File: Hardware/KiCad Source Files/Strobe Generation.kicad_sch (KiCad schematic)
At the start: 23 parts, among them Q1 IRLU024NPBF, Q2 IRLU024NPBF, Q3 Q_NMOS

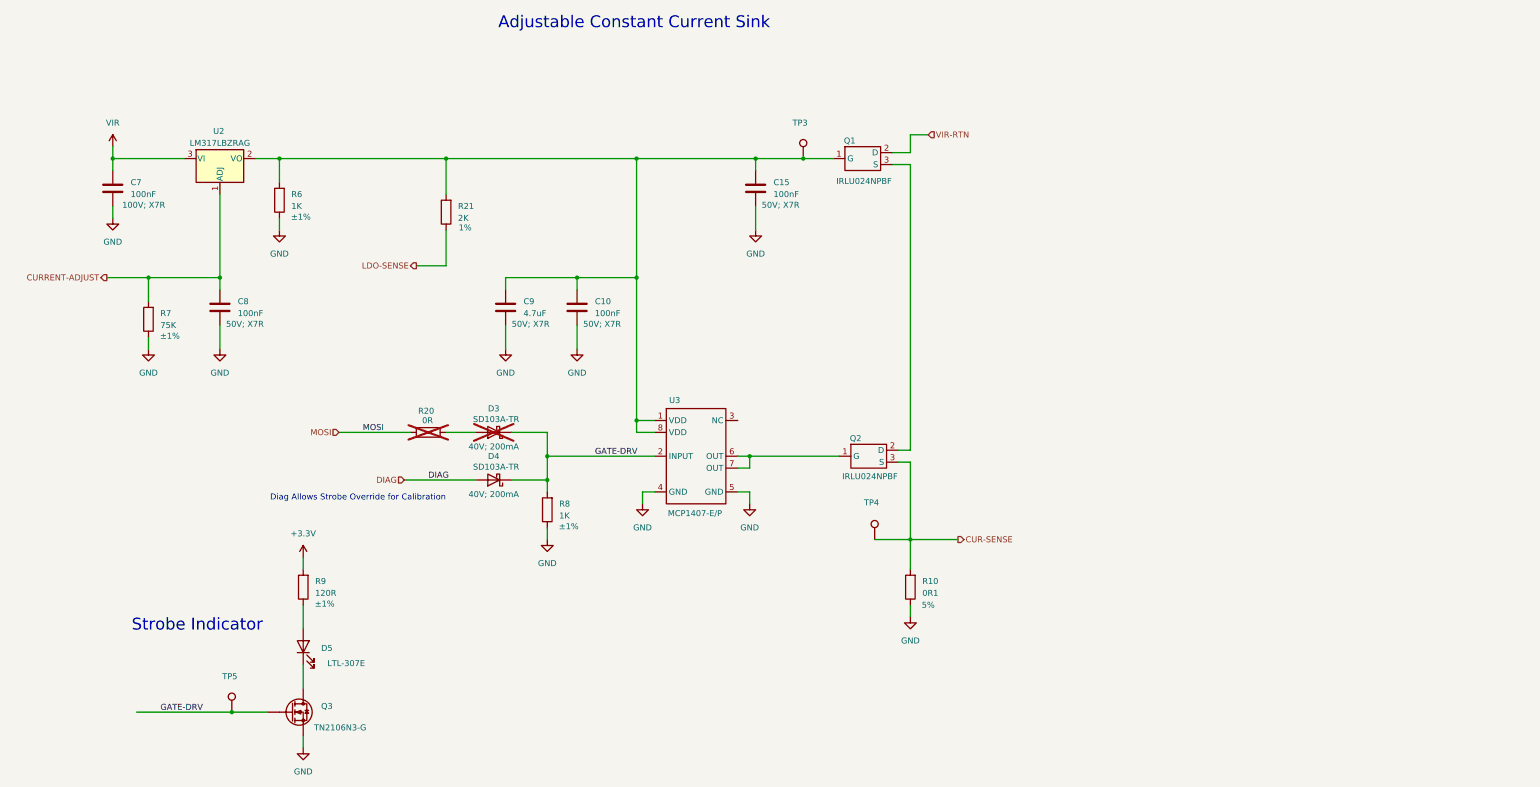
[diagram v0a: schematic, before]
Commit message: V3 connector board: strobe pulse limiter, USB-C fixes, boost protection
Mechanical: board outline, all mounting/tab/breakaway holes and every
existing part position are unchanged (checked against the previous revision);
all new parts are on the top side and no taller than existing parts.
PiTrac software compatibility: the LED current-control circuit and the
DAC/ADC/DIAG interface used by strobe_calibration_manager.py are unchanged.

Strobe (CC Sink sheet)
- AC-coupled pulse limiter: TRIG (DIAG/MOSI via D3/D4) -> C16 220nF ->
  GATE-DRV, R28 10K to GND (tau 2.2 ms). 8.7-130 us strobes and the
  calibration pulse pass (guaranteed >= ~0.38 ms by the MCP1407 input
  limits); a stuck-high DIAG turns the driver off after ~1.7 ms typical,
  <= ~2.8 ms worst case, so 10 A can no longer be held on.

USB-C (Connectors sheet, USB4085-GF-A footprint)
- J2/J5 feed 5 V to the Pis: add 10K Rp on CC1/CC2 (R24-R27, 1206).
- Footprint rebuilt to GCT's land pattern (16 plated 0.40/0.66 mm pins).
  The old VBUS/GND pads had 0.1 mm top-side copper (annular-ring DRC
  errors; Pi supply current only reached them via the barrel/bottom pad).

Boost (Power sheet)
- F1 MF-MSMF050-2 polyfuse in the boost input only (+5V_BST: C1/C2/C3/R1/
  U1); PCB: +5V_BST F.Cu island, +5V B.Cu bridge keeps the Pi feed width.
- D16 P4SMA39CA clamp on VIR (open-feedback fault; relies on F1).
- R5 2K49 -> 10K (was ~0.45 W in a 1/4 W resistor).

Housekeeping
- Project sym/fp-lib-tables; USB4085-GF-A added to the symbol library;
  pin types for custom parts; locally modified Q_NPN/Q_NMOS/LED moved into
  the project library (Q_NPN_EBC, Q_NMOS_SGD, LED_ThermalPad) to keep their
  numeric pinouts; no-connect flags; PWR_FLAGs; GATE-DRV wire to Q3 fixed.
- ERC pin map (project-wide): open emitter on a power rail allowed
  (MC33063 SwE to GND).
- Add V3 Connector Only.kicad_pro (board had no rules; DRC used defaults).
- Breakaway holes marked board-only.
- Regenerated Gerber/drill zips, BOM and centroid CSVs (same for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
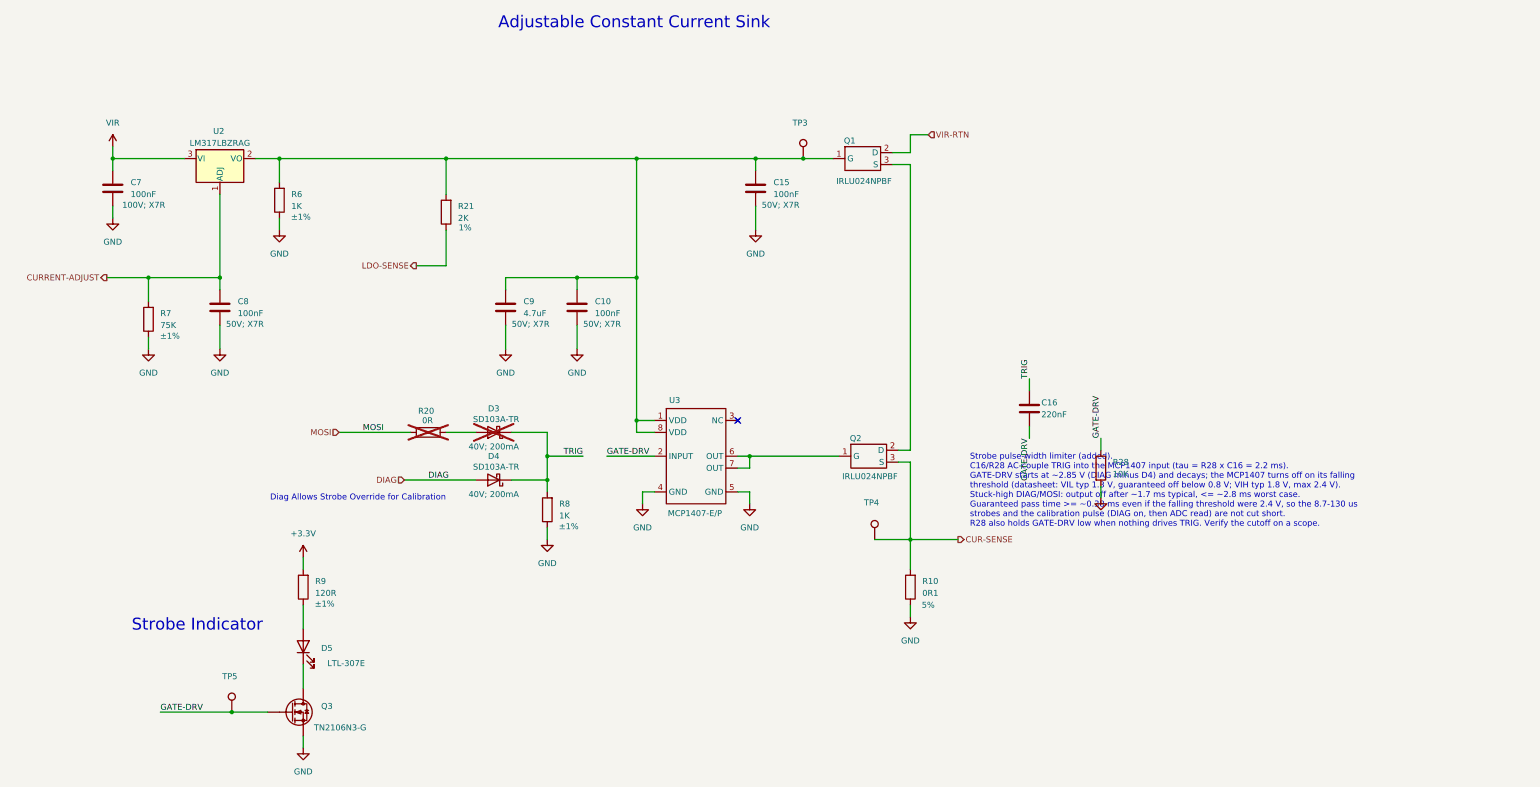
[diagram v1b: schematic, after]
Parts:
- added C16: 220nF, Capacitor_THT:C_Disc_D4.3mm_W1.9mm_P5.00mm, symbol Device:C
- added R28: 10K, Resistor_THT:R_Axial_DIN0207_L6.3mm_D2.5mm_P2.54mm_Vertical, symbol Device:R
- Q3: symbol Device:Q_NMOS -> Pi Connector Parts:Q_NMOS_SGD
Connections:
- net GATE-DRV: now also C16.2, R28.1; no longer D3.1 (K), D4.1 (K), R8.2
- net GND: now also R28.2
- new net TRIG: C16.1, D3.1 (K), D4.1 (K), R8.2
- no-connect marks 0 -> 1
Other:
- note added: "Strobe pulse-width limiter (added). C16/R28 AC-couple TRIG into the MCP1407 input (tau = R28 x C16 = 2.2 ms). GATE-DRV starts at ~2.85 V (DIAG minus D4) and decays; the MCP1407 turns off on its falling threshold (datasheet: VIL typ 1.3 V, guaranteed off below 0.8 V; VIH typ 1.8 V, max 2.4 V). Stuck-high DIAG/MOSI: output off after ~1.7 ms typical, <= ~2.8 ms worst case. Guaranteed pass time >= ~0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"

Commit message: C16: use an orderable part (K224K20X7RF5UH5, 220nF 50V X7R)
K224K15X7RF5UH5 isn't listed by any distributor; the "20" (50 V) code is the
real 220 nF part in this Vishay K series (DigiKey 2356767, element14
2860121). Footprint moved to C_Disc_D5.1mm_W3.2mm_P5.00mm, the one already
used for C2 (1 uF in the same series), so the body fits.
Outputs regenerated; ERC/DRC unchanged (0 errors), geometry unchanged.

Co-Authored-By: Claude Opus 5.5 <noreply@anthropic.com>
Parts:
- C16: footprint Capacitor_THT:C_Disc_D4.3mm_W1.9mm_P5.00mm -> Capacitor_THT:C_Disc_D5.1mm_W3.2mm_P5.00mm; Part Number K224K15X7RF5UH5 -> K224K20X7RF5UH5
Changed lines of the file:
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@@
 			)
 		)
-		(property "Footprint" "Capacitor_THT:C_Disc_D4.3mm_W1.9mm_P5.00mm"
+		(property "Footprint" "Capacitor_THT:C_Disc_D5.1mm_W3.2mm_P5.00mm"
 			(at 241.3 104.14 0)
 			(effects
@@
 			)
 		)
-		(property "Part Number" "K224K15X7RF5UH5"
+		(property "Part Number" "K224K20X7RF5UH5"
 			(at 241.3 104.14 0)
 			(effects

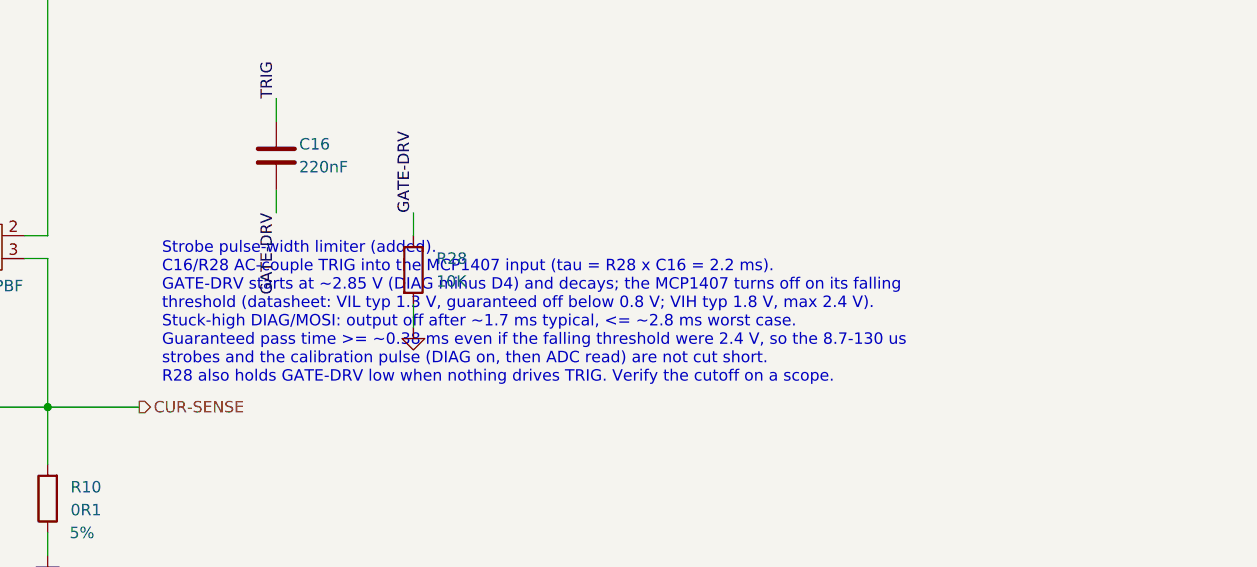
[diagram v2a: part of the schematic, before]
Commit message: Address PR review: R5 part number, timing bounds, library defaults, ERC scope
- R5: PCB Part Number field still named the old MFR-25FTE52-2K49 on both
  boards; now MFR-25FRF52-10K, matching the schematic and BOM. (The stage-A
  update changed the value but not the BOM fields; no other part drifted.)
- Limiter note: worst-case bounds now include R28 1%, C16 +-10% plus X7R
  drift and a 2.7-2.95 V start level: cutoff <= ~3.2 ms, pass >= ~0.2 ms
  worst case (~1.7 ms typical for both).
- USB-C labels: "3A advertised (CC), 5A max" instead of "5A" — the Rp
  pull-ups advertise Type-C 3 A; the connector/copper are rated 5 A.
- Project library: default references Q4/Q1/D1 -> Q/Q/D; LED_ThermalPad
  default footprint -> Pi Connector Parts:VSMA1085400 (was an unresolvable
  Library:SST-10-IRD-B90H-S810). Sheet caches updated identically.
- ERC: revert the project-wide open-emitter/power-output relaxation and add a
  single exclusion for U1 pin 2 (MC33063 SwE to GND).
- V3 Connector Only.kicad_pro: own export folder and BOM file name.
- Regenerated Gerber zips and schematic PDF (BOM/centroid unchanged).

ERC 0 (1 intended exclusion). DRC both boards: 0 errors.

Co-Authored-By: Claude Opus 5.5 <noreply@anthropic.com>
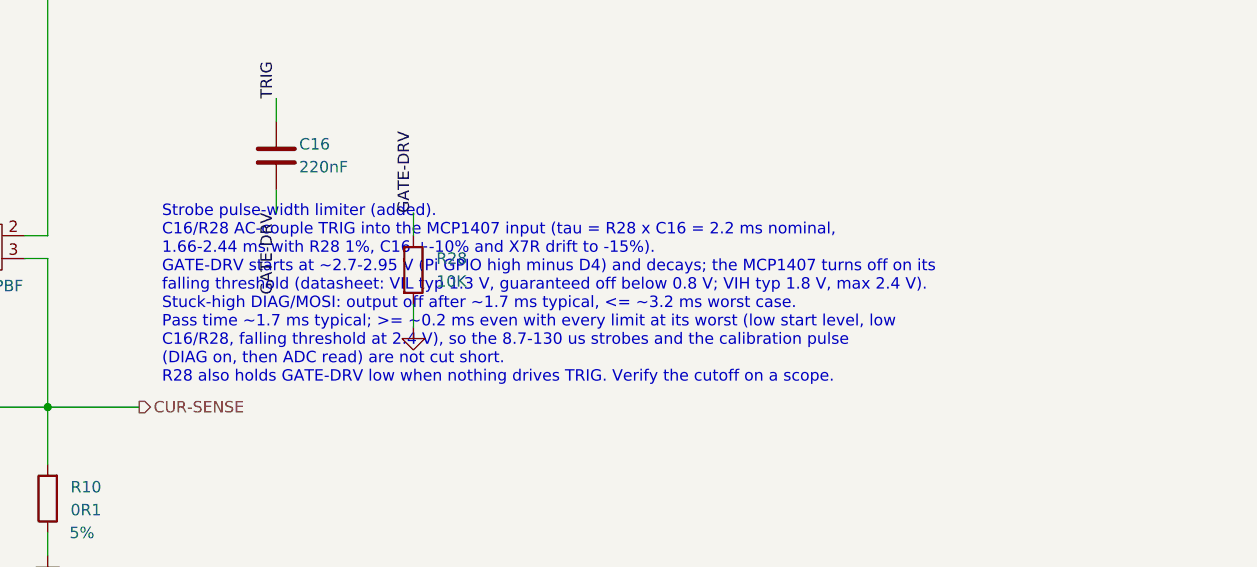
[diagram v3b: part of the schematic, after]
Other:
- note added: "Strobe pulse-width limiter (added). C16/R28 AC-couple TRIG into the MCP1407 input (tau = R28 x C16 = 2.2 ms nominal, 1.66-2.44 ms with R28 1%, C16 +-10% and X7R drift to -15%). GATE-DRV starts at ~2.7-2.95 V (Pi GPIO high minus D4) and decays; the MCP1407 turns off on its falling threshold (datasheet: VIL typ 1.3 V, guaranteed off below 0.8 V; VIH typ 1.8 V, max 2.4 V). Stuck-high DIAG/MOSI: outp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"
- note removed: "Strobe pulse-width limiter (added). C16/R28 AC-couple TRIG into the MCP1407 input (tau = R28 x C16 = 2.2 ms). GATE-DRV starts at ~2.85 V (DIAG minus D4) and decays; the MCP1407 turns off on its falling threshold (datasheet: VIL typ 1.3 V, guaranteed off below 0.8 V; VIH typ 1.8 V, max 2.4 V). Stuck-high DIAG/MOSI: output off after ~1.7 ms typical, <= ~2.8 ms worst case. Guaranteed pass time >= ~0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"
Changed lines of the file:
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@@
 		)
 	)
-	(text "Strobe pulse-width limiter (added).
-C16/R28 AC-couple TRIG into the MCP1407 input (tau = R28 x C16 = 2.2 ms).
-GATE-DRV starts at ~2.85 V (DIAG minus D4) and decays; the MCP1407 turns off on its falling
-threshold (datasheet: VIL typ 1.3 V, guaranteed off below 0.8 V; VIH typ 1.8 V, max 2.4 V).
-Stuck-high DIAG/MOSI: output off after ~1.7 ms typical, <= ~2.8 ms worst case.
-Guaranteed pass time >= ~0.38 ms even if the falling threshold were 2.4 V, so the 8.7-130 us
-strobes and the calibration pulse (DIAG on, then ADC read) are not cut short.
-R28 also holds GATE-DRV low when nothing drives TRIG. Verify the cutoff on a scope."
+	(text "Strobe pulse-width limiter (added).\nC16/R28 AC-couple TRIG into the MCP1407 input (tau = R28 x C16 = 2.2 ms nominal,\n1.66-2.44 ms with R28 1%, C16 +-10% and X7R drift to -15%).\nGATE-DRV starts at ~2.7-2.95 V (Pi GPIO high minus D4) and decays; the MCP1407 turns off on its\nfalling threshold (datasheet: VIL typ 1.3 V, guaranteed off below 0.8 V; VIH typ 1.8 V, max 2.4 V).\nStuck-high DIAG/MOSI: output off after ~1.7 ms typical, <= ~3.2 ms worst case.\nPass time ~1.7 ms typical; >= ~0.2 ms even with every limit at its worst (low start level, low\nC16/R28, falling threshold at 2.4 V), so the 8.7-130 us strobes and the calibration pulse\n(DIAG on, then ADC read) are not cut short.\nR28 also holds GATE-DRV low when nothing drives TRIG. Verify the cutoff on a scope."
 		(exclude_from_sim no)
 		(at 228.6 129.54 0)
